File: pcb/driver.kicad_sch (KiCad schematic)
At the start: 1 part, among them U1 DRV8847RTE

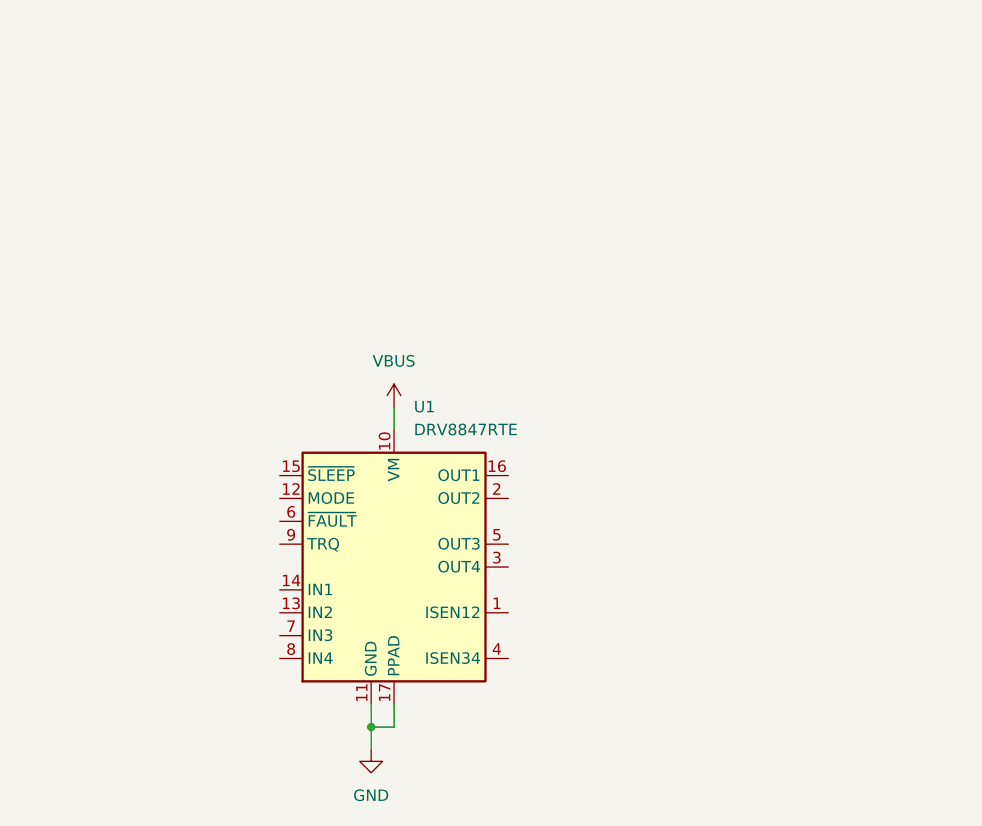
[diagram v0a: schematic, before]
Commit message: Finish schematic
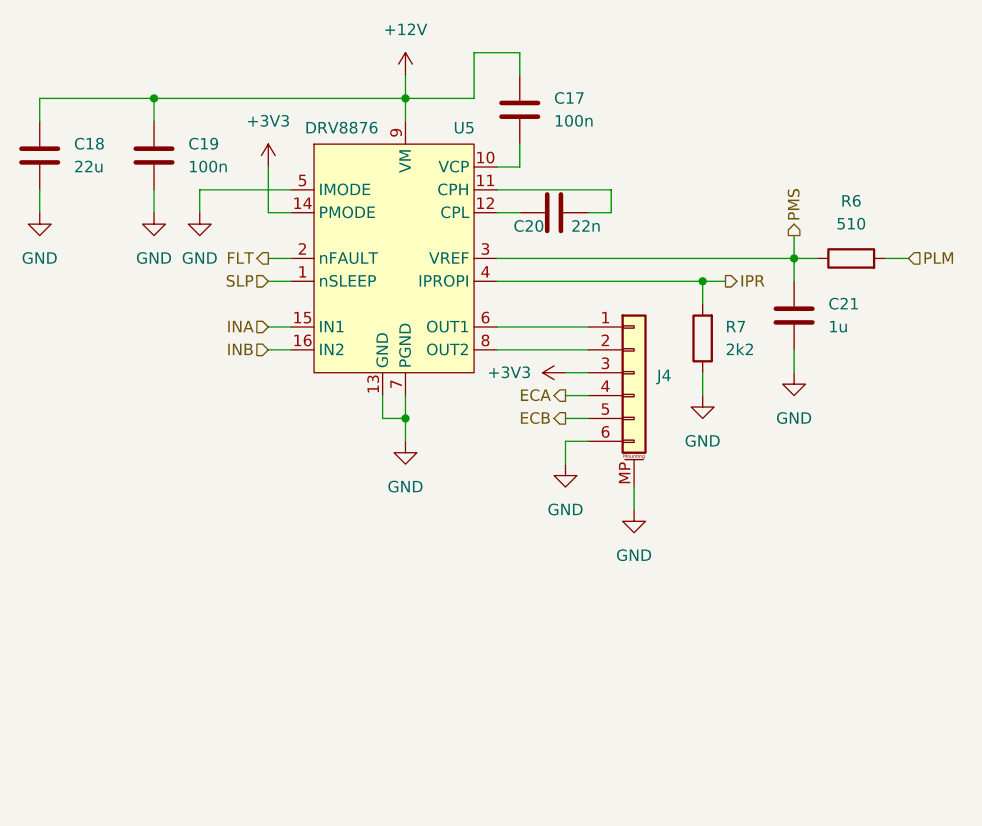
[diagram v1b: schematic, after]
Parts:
- removed U1: DRV8847RTE, Package_DFN_QFN:QFN-16-1EP_3x3mm_P0.5mm_EP1.7x1.7mm_ThermalVias, symbol Driver_Motor:DRV8847RTE
- added C17, C19: 100n, Capacitor_SMD:C_0402_1005Metric, symbol Device:C
- added C18: 22u, Capacitor_SMD:C_1206_3216Metric, symbol Device:C
- added C20: 22n, Capacitor_SMD:C_0402_1005Metric, symbol Device:C
- added C21: 1u, Capacitor_SMD:C_0402_1005Metric, symbol Device:C
- added J4: Conn_01x06_MountingPin, Connector_JST:JST_SH_SM06B-SRSS-TB_1x06-1MP_P1.00mm_Horizontal, symbol Connector_Generic_MountingPin:Conn_01x06_MountingPin
- added R6: 510, Resistor_SMD:R_0402_1005Metric, symbol Device:R
- added R7: 2k2, Resistor_SMD:R_0402_1005Metric, symbol Device:R
- added U5: DRV8876, Package_DFN_QFN:QFN-16-1EP_3x3mm_P0.5mm_EP1.7x1.7mm_ThermalVias, symbol User_Symbols:DRV8876
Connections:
- net GND: now also C18.2, C19.2, C21.2, J4.6 (Pin_6), J4.MP (MountPin), R7.1, U5.13 (GND), U5.17 (PAD), U5.5 (IMODE), U5.7 (PGND)
- new net: C17.2, U5.10 (VCP)
- new net: C20.1, U5.11 (CPH)
- new net: C20.2, U5.12 (CPL)
- new net: J4.1 (Pin_1), U5.6 (OUT1)
- new net: J4.2 (Pin_2), U5.8 (OUT2)
- new net +12V: C17.1, C18.1, C19.1, U5.9 (VM)
- new net +3V3: J4.3 (Pin_3), U5.14 (PMODE)
- new net ECA: J4.4 (Pin_4)
- new net ECB: J4.5 (Pin_5)
- new net FLT: U5.2 (nFAULT)
- new net INA: U5.15 (IN1)
- new net INB: U5.16 (IN2)
- new net IPR: R7.2, U5.4 (IPROPI)
- new net PLM: R6.2
- new net PMS: C21.1, R6.1, U5.3 (VREF)
- new net SLP: U5.1 (nSLEEP)

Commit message: Random save
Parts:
- J4: LCSC (none) -> C160405
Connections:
- net OUT1: now reaches J4.1 (Pin_1), U5.6 (OUT1)
- net OUT2: now reaches J4.2 (Pin_2), U5.8 (OUT2)
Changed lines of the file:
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@@
+		)
+	)
+	(label "OUT1"
+		(at 110.49 68.58 0)
+		(fields_autoplaced yes)
+		(effects
+			(font
+				(size 1.27 1.27)
+			)
+			(justify left bottom)
+		)
+	)
+	(label "OUT2"
+		(at 110.49 71.12 0)
+		(fields_autoplaced yes)
+		(effects
+			(font
+				(size 1.27 1.27)
+			)
+			(justify left bottom)
 		)
 	)
@@
 			(at 121.92 73.66 0)
 			(effects
+				(font
+					(size 1.27 1.27)
+				)
+				(hide yes)
+			)
+		)
+		(property "LCSC" "C160405"
+			(at 121.92 73.66 0)
+			(effects

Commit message: Add inserts and change CAN connection
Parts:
- renumbered C17 to C27, C18 to C28, C19 to C29, C20 to C30, C21 to C31, J4 to J6, R6 to R10, R7 to R11, U5 to U7
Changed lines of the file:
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@@
 		(dnp no)
 		(fields_autoplaced yes)
-		(property "Reference" "C19"
+		(property "Reference" "C29"
 			(at 72.39 48.2599 0)
 			(effects
@@
 		(dnp no)
 		(fields_autoplaced yes)
-		(property "Reference" "R6"
+		(property "Reference" "R10"
 			(at 146.05 54.61 90)
 			(effects
@@
 		(dnp no)
 		(fields_autoplaced yes)
-		(property "Reference" "#PWR032"
+		(property "Reference" "#PWR054"
 			(at 96.52 44.45 0)
 			(effects
@@
 		(on_board yes)
 		(dnp no)
-		(property "Reference" "U5"
+		(property "Reference" "U7"
 			(at 101.854 46.482 0)
 			(effects
@@
 		(dnp no)
 		(fields_autoplaced yes)
-		(property "Reference" "#PWR037"
+		(property "Reference" "#PWR059"
 			(at 118.11 73.66 0)
 			(effects
@@
 		(dnp no)
 		(fields_autoplaced yes)
-		(property "Reference" "R7"
+		(property "Reference" "R11"
 			(at 132.08 68.5799 0)
 			(effects
@@
 		(dnp no)
 		(fields_autoplaced yes)
-		(property "Reference" "#PWR039"
+		(property "Reference" "#PWR061"
 			(at 129.54 82.55 0)
 			(effects
@@
 		(on_board yes)
 		(dnp no)
-		(property "Reference" "C20"
+		(property "Reference" "C30"
 			(at 110.236 57.404 90)
 			(effects
@@
 		(dnp no)
 		(fields_autoplaced yes)
-		(property "Reference" "#PWR041"
+		(property "Reference" "#PWR063"
 			(at 114.3 90.17 0)
 			(effects
@@
 		(dnp no)
 		(fields_autoplaced yes)
-		(property "Reference" "C21"
+		(property "Reference" "C31"
 			(at 143.51 66.0399 0)
 			(effects
@@
 		(dnp no)
 		(fields_autoplaced yes)
-		(property "Reference" "#PWR035"
+		(property "Reference" "#PWR057"
 			(at 68.58 62.23 0)
 			(effects
@@
 		(dnp no)
 		(fields_autoplaced yes)
-		(property "Reference" "C17"
+		(property "Reference" "C27"
 			(at 113.03 43.1799 0)
 			(effects
@@
 		(dnp no)
 		(fields_autoplaced yes)
-		(property "Reference" "#PWR034"
+		(property "Reference" "#PWR056"
 			(at 55.88 62.23 0)
 			(effects
@@
 		(dnp no)
 		(fields_autoplaced yes)
-		(property "Reference" "#PWR036"
+		(property "Reference" "#PWR058"
 			(at 73.66 62.23 0)
 			(effects
@@
 		(dnp no)
 		(fields_autoplaced yes)
-		(property "Reference" "#PWR040"
+		(property "Reference" "#PWR062"
 			(at 96.52 87.63 0)
 			(effects
@@
 		(dnp no)
 		(fields_autoplaced yes)
-		(property "Reference" "#PWR042"
+		(property "Reference" "#PWR064"
 			(at 121.92 95.25 0)
 			(effects
@@
 		(dnp no)
 		(fields_autoplaced yes)
-		(property "Reference" "#PWR038"
+		(property "Reference" "#PWR060"
 			(at 139.7 80.01 0)
 			(effects
@@
 		(dnp no)
 		(fields_autoplaced yes)
-		(property "Reference" "#PWR033"
+		(property "Reference" "#PWR055"
 			(at 81.28 54.61 0)
 			(effects
@@
 		(dnp no)
 		(fields_autoplaced yes)
-		(property "Reference" "C18"
+		(property "Reference" "C28"
 			(at 59.69 48.2599 0)
 			(effects
@@
 		(dnp no)
 		(fields_autoplaced yes)
-		(property "Reference" "J4"
+		(property "Reference" "J6"
 			(at 124.46 74.0155 0)
 			(effects

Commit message: Finish routing and rule checking
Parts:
- C31: value 1u -> 10u; LCSC (none) -> C15525
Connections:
- net PMS: no longer names the net of C31.1, R10.1, U7.3 (VREF)
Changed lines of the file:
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@@
-	(wire
-		(pts
-			(xy 139.7 58.42) (xy 139.7 60.96)
-		)
-		(stroke
-			(width 0)
-			(type default)
-		)
-	)
 	(wire
 		(pts
@@
 	(wire
 		(pts
+			(xy 55.88 53.34) (xy 55.88 55.88)
+		)
+		(stroke
+			(width 0)
+			(type default)
+		)
+	)
+	(wire
+		(pts
+			(xy 121.92 88.9) (xy 121.92 86.36)
+		)
+		(stroke
+			(width 0)
+			(type default)
+		)
+	)
+	(wire
+		(pts
+			(xy 114.3 83.82) (xy 114.3 81.28)
+		)
+		(stroke
+			(width 0)
+			(type default)
+		)
+	)
+	(wire
+		(pts
+			(xy 68.58 45.72) (xy 68.58 43.18)
+		)
+		(stroke
+			(width 0)
+			(type default)
+		)
+	)
+	(wire
+		(pts
+			(xy 73.66 53.34) (xy 83.82 53.34)
+		)
+		(stroke
+			(width 0)
+			(type default)
+		)
+	)
+	(wire
+		(pts
+			(xy 81.28 60.96) (xy 83.82 60.96)
+		)
+		(stroke
+			(width 0)
+			(type default)
+		)
+	)
+	(wire
+		(pts
+			(xy 93.98 76.2) (xy 93.98 78.74)
+		)
+		(stroke
+			(width 0)
+			(type default)
+		)
+	)
+	(wire
+		(pts
+			(xy 109.22 38.1) (xy 104.14 38.1)
+		)
+		(stroke
+			(width 0)
+			(type default)
+		)
+	)
+	(wire
+		(pts
+			(xy 106.68 53.34) (xy 119.38 53.34)
+		)
+		(stroke
+			(width 0)
+			(type default)
+		)
+	)
+	(wire
+		(pts
 			(xy 106.68 60.96) (xy 139.7 60.96)
-		)
-		(stroke
-			(width 0)
-			(type default)
-		)
-	)
-	(wire
-		(pts
-			(xy 55.88 53.34) (xy 55.88 55.88)
-		)
-		(stroke
-			(width 0)
-			(type default)
-		)
-	)
-	(wire
-		(pts
-			(xy 121.92 88.9) (xy 121.92 86.36)
-		)
-		(stroke
-			(width 0)
-			(type default)
-		)
-	)
-	(wire
-		(pts
-			(xy 114.3 83.82) (xy 114.3 81.28)
-		)
-		(stroke
-			(width 0)
-			(type default)
-		)
-	)
-	(wire
-		(pts
-			(xy 68.58 45.72) (xy 68.58 43.18)
-		)
-		(stroke
-			(width 0)
-			(type default)
-		)
-	)
-	(wire
-		(pts
-			(xy 73.66 53.34) (xy 83.82 53.34)
-		)
-		(stroke
-			(width 0)
-			(type default)
-		)
-	)
-	(wire
-		(pts
-			(xy 81.28 60.96) (xy 83.82 60.96)
-		)
-		(stroke
-			(width 0)
-			(type default)
-		)
-	)
-	(wire
-		(pts
-			(xy 93.98 76.2) (xy 93.98 78.74)
-		)
-		(stroke
-			(width 0)
-			(type default)
-		)
-	)
-	(wire
-		(pts
-			(xy 109.22 38.1) (xy 104.14 38.1)
-		)
-		(stroke
-			(width 0)
-			(type default)
-		)
-	)
-	(wire
-		(pts
-			(xy 106.68 53.34) (xy 119.38 53.34)
 		)
 		(stroke
@@
 			)
 			(justify right)
-		)
-	)
-	(hierarchical_label "PMS"
-		(shape output)
-		(at 139.7 58.42 90)
-		(fields_autoplaced yes)
-		(effects
-			(font
-				(size 1.27 1.27)
-			)
-			(justify left)
 		)
 	)
@@
 			)
 		)
-		(property "Value" "1u"
+		(property "Value" "10u"
 			(at 143.51 68.5799 0)
 			(effects
@@
 			(at 139.7 67.31 0)
 			(effects
+				(font
+					(size 1.27 1.27)
+				)
+				(hide yes)
+			)
+		)
+		(property "LCSC" "C15525"
+			(at 139.7 67.31 0)
+			(effects

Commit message: Save
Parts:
- U7: LCSC (none) -> C1852100
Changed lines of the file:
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@@
+			)
+		)
+		(property "LCSC" "C1852100"
+			(at 86.36 50.8 0)
+			(effects
+				(font
+					(size 1.27 1.27)
+				)
+				(hide yes)
 			)
 		)

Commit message: Make revision 2
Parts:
- C30: LCSC (none) -> C1532
- R10: LCSC (none) -> C25123
- R11: LCSC (none) -> C25879
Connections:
- net SLP is gone; now on net +3V3: U7.1 (nSLEEP)
- net FLT: no longer names the net of U7.2 (nFAULT)
- no-connect marks 0 -> 1
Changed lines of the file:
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@@
 		(color 0 0 0 0)
 	)
+	(junction
+		(at 81.28 55.88)
+		(diameter 0)
+		(color 0 0 0 0)
+	)
+	(no_connect
+		(at 83.82 60.96)
+	)
 	(wire
 		(pts
@@
 	(wire
 		(pts
+			(xy 81.28 55.88) (xy 81.28 63.5)
+		)
+		(stroke
+			(width 0)
+			(type default)
+		)
+	)
+	(wire
+		(pts
 			(xy 96.52 78.74) (xy 96.52 81.28)
 		)
@@
 		(pts
 			(xy 73.66 53.34) (xy 83.82 53.34)
-		)
-		(stroke
-			(width 0)
-			(type default)
-		)
-	)
-	(wire
-		(pts
-			(xy 81.28 60.96) (xy 83.82 60.96)
 		)
 		(stroke
@@
 		)
 	)
-	(hierarchical_label "SLP"
-		(shape input)
-		(at 81.28 63.5 180)
+	(hierarchical_label "IPR"
+		(shape output)
+		(at 132.08 63.5 0)
 		(fields_autoplaced yes)
 		(effects
@@
 				(size 1.27 1.27)
 			)
-			(justify right)
-		)
-	)
-	(hierarchical_label "IPR"
-		(shape output)
-		(at 132.08 63.5 0)
+			(justify left)
+		)
+	)
+	(hierarchical_label "INA"
+		(shape input)
+		(at 81.28 68.58 180)
 		(fields_autoplaced yes)
 		(effects
@@
 				(size 1.27 1.27)
 			)
-			(justify left)
-		)
-	)
-	(hierarchical_label "INA"
+			(justify right)
+		)
+	)
+	(hierarchical_label "INB"
 		(shape input)
-		(at 81.28 68.58 180)
+		(at 81.28 71.12 180)
 		(fields_autoplaced yes)
 		(effects
@@
 		)
 	)
-	(hierarchical_label "INB"
-		(shape input)
-		(at 81.28 71.12 180)
-		(fields_autoplaced yes)
-		(effects
-			(font
-				(size 1.27 1.27)
-			)
-			(justify right)
-		)
-	)
 	(hierarchical_label "ECA"
 		(shape output)
 		(at 114.3 76.2 180)
-		(fields_autoplaced yes)
-		(effects
-			(font
-				(size 1.27 1.27)
-			)
-			(justify right)
-		)
-	)
-	(hierarchical_label "FLT"
-		(shape output)
-		(at 81.28 60.96 180)
 		(fields_autoplaced yes)
 		(effects
@@
 		(property "Description" "Resistor"
 			(at 146.05 60.96 0)
+			(effects
+				(font
+					(size 1.27 1.27)
+				)
+				(hide yes)
+			)
+		)
+		(property "LCSC" "C25123"
+			(at 146.05 60.96 90)
 			(effects
 				(font
@@
 			)
 		)
+		(property "LCSC" "C25879"
+			(at 129.54 69.85 0)
+			(effects
+				(font
+					(size 1.27 1.27)
+				)
+				(hide yes)
+			)
+		)
 		(pin "1"
 		)
@@
 			(effects
 				(font
+					(size 1.27 1.27)
+				)
+				(hide yes)
+			)
+		)
+		(property "LCSC" "C1532"
+			(at 113.03 55.88 90)
+			(effects
+				(font
